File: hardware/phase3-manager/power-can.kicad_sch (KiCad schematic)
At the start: 23 parts, among them J1 BACKPLANE, Q8 2N7002, U11 TCAN1042HGV, U8 LMR36015AQRNXRQ1, U9 NCP1117-3.3

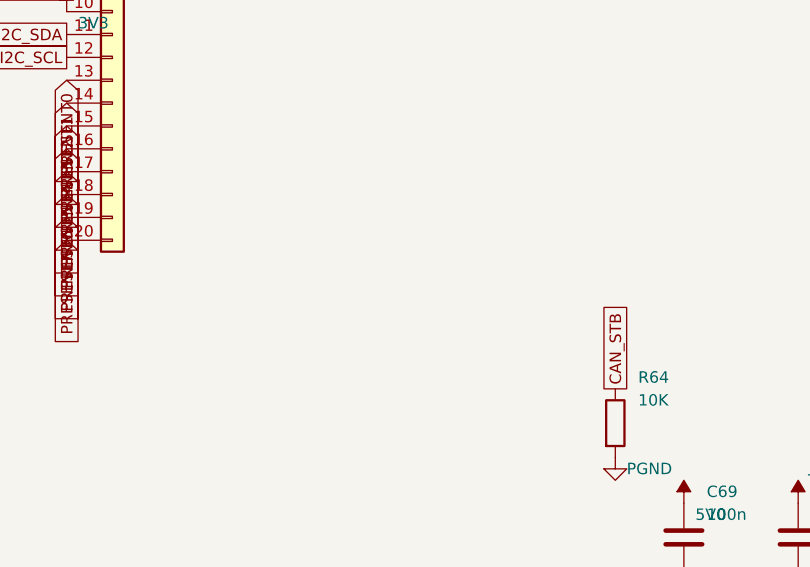
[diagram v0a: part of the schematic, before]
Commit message: Phase-3 schematic audit: real find fixed (manager I2C pull-ups), SPICE clean
The analyzer caught a genuine capture omission: docs/09 s.3 specifies 4.7K
I2C pull-ups on the manager (it owns the bus feeding TCA9535 + the
backplane INA228), but gen_manager.py never drew them - and EXPECTED_NETS,
written from the same plan, shared the blind spot. R62/R63 added, all
checkers re-verified green (80 components).

Triage of the rest:
- backplane PR-001/PU-001 "missing I2C pull-ups": by design, manager owns
  them (docs/09); U1 ALERT unused open-drain, no pull needed
- RS-001: PWR_FLAG-invisible analyzer class (accepted since Phase-1)
- SS-001/DS: MPN pass deferred to the batch BOM stage as before
ngspice: manager 16/16 pass, backplane 3/3 pass (0 warn, 0 fail, 0 skip).
Analysis manifests tracked per convention.

Co-Authored-By: Claude Fable 5 <noreply@anthropic.com>
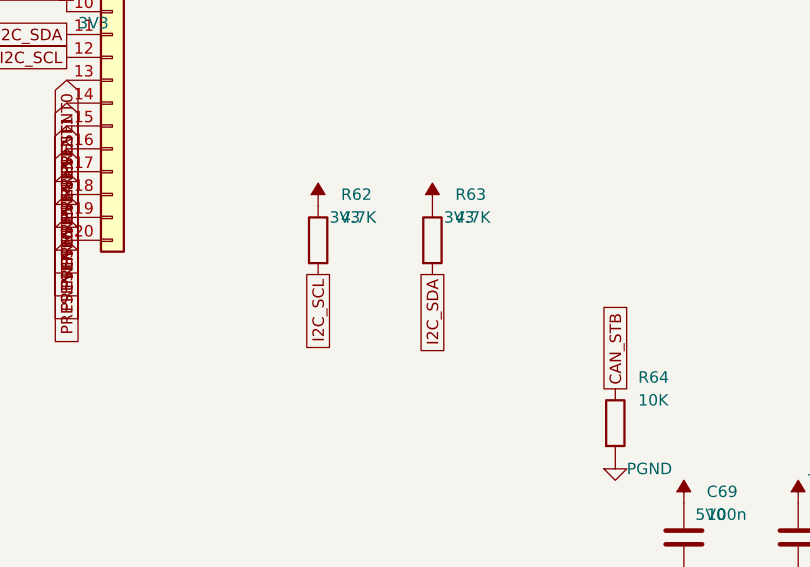
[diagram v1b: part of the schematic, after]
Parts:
- added R62, R63: 4.7K, Resistor_SMD:R_0603_1608Metric, symbol Device:R
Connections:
- net 3V3: now also R62.1, R63.1
- net I2C_SCL: now also R62.2
- net I2C_SDA: now also R63.2

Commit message: Add LCSC part numbers to all four boards' schematics and generate BOMs
common/bom.py writes hidden LCSC/MPN/Manufacturer properties into the
placed symbols (additive only, both one-line and KiCad multi-line
property styles) and emits <board>/bom/<board>-bom.csv plus a
JLCPCB-format CSV. Part table in common/lcsc_parts.py, transcribed
from SOURCING.md with explicit references per board; CHECK notes flag
footprint/variant mismatches. --check fails on stale output.

Co-Authored-By: Claude Opus 5.5 (1M context) <noreply@anthropic.com>
Claude-Session: https://claude.ai/code/session_01MKtKgebN9BpUrgqHq9t7pT
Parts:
- F1: LCSC (none) -> C3207114
- U11: LCSC (none) -> C485806; MPN (none) -> TCAN1042VDRQ1; Manufacturer (none) -> TI
- U8: LCSC (none) -> C1850345; MPN (none) -> LMR36015ARNXR; Manufacturer (none) -> TI
- U9: LCSC (none) -> C26537; MPN (none) -> NCP1117ST33T3G; Manufacturer (none) -> onsemi
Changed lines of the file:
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@@
     (property "Footprint" "Fuse:Fuse_Blade_Mini_directSolder" (at 63.5 55.88 0) (effects (font (size 1.27 1.27)) hide))
     (property "Datasheet" "~" (at 63.5 55.88 0) (effects (font (size 1.27 1.27)) hide))
+    (property "LCSC" "C3207114" (at 63.5 55.88 0) (effects (font (size 1.27 1.27)) hide))
     (pin "1")
     (pin "2")
@@
     (property "Footprint" "labbench:LMR36015_RNX_VQFN-HR-12" (at 116.84 78.74 0) (effects (font (size 1.27 1.27)) hide))
     (property "Datasheet" "~" (at 116.84 78.74 0) (effects (font (size 1.27 1.27)) hide))
+    (property "LCSC" "C1850345" (at 116.84 78.74 0) (effects (font (size 1.27 1.27)) hide))
+    (property "MPN" "LMR36015ARNXR" (at 116.84 78.74 0) (effects (font (size 1.27 1.27)) hide))
+    (property "Manufacturer" "TI" (at 116.84 78.74 0) (effects (font (size 1.27 1.27)) hide))
     (pin "1")
     (pin "10")
@@
     (property "Footprint" "Package_TO_SOT_SMD:SOT-223-3_TabPin2" (at 218.44 78.74 0) (effects (font (size 1.27 1.27)) hide))
     (property "Datasheet" "~" (at 218.44 78.74 0) (effects (font (size 1.27 1.27)) hide))
+    (property "LCSC" "C26537" (at 218.44 78.74 0) (effects (font (size 1.27 1.27)) hide))
+    (property "MPN" "NCP1117ST33T3G" (at 218.44 78.74 0) (effects (font (size 1.27 1.27)) hide))
+    (property "Manufacturer" "onsemi" (at 218.44 78.74 0) (effects (font (size 1.27 1.27)) hide))
     (pin "1")
     (pin "2")
@@
     (property "Footprint" "Package_SO:SOIC-8_3.9x4.9mm_P1.27mm" (at 116.84 152.4 0) (effects (font (size 1.27 1.27)) hide))
     (property "Datasheet" "~" (at 116.84 152.4 0) (effects (font (size 1.27 1.27)) hide))
-    (pin "1")
-    (pin "2")
+    (property "LCSC" "C485806" (at 116.84 152.4 0) (effects (font (size 1.27 1.27)) hide))
+    (property "MPN" "TCAN1042VDRQ1" (at 116.84 152.4 0) (effects (font (size 1.27 1.27)) hide))
+    (property "Manufacturer" "TI" (at 116.84 152.4 0) (effects (font (size 1.27 1.27)) hide))
+    (pin "1")
+    (pin "2")

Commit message: Fix manager ENC1, F1 and BZ1 part numbers to fit their existing lands
- ENC1: C2831776 was a 100 uF/50 V electrolytic, not an encoder. Now Alps
  EC11E18244A5 (C255515), the EC11E with push switch the footprint is for.
- F1: C3207114 was a 6.35 mm cylindrical fuse clip. The land is a
  direct-solder MINI blade, so F1 is now the 2 A fuse itself, Littelfuse
  0297002.WXNV (C151091). The Phase-1 F1 note is corrected the same way.
- BZ1: MLT-8530 is rated 2.5-4.5 V but runs from 5V0. Now YX-SMD8530P
  (C781886), rated 2-5 V, with the same vendor land and pad-1 (+) corner.

Schematic LCSC/MPN fields and BOM CSVs regenerated with common/bom.py.
No footprint or layout change.

Co-Authored-By: Claude Opus 5.5 (1M context) <noreply@anthropic.com>
Claude-Session: https://claude.ai/code/session_01Ekhw9jYnrfxihP7yvxax5H
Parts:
- F1: LCSC C3207114 -> C151091; MPN (none) -> 0297002.WXNV; Manufacturer (none) -> Littelfuse
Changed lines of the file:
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@@
     (property "Footprint" "Fuse:Fuse_Blade_Mini_directSolder" (at 63.5 55.88 0) (effects (font (size 1.27 1.27)) hide))
     (property "Datasheet" "~" (at 63.5 55.88 0) (effects (font (size 1.27 1.27)) hide))
-    (property "LCSC" "C3207114" (at 63.5 55.88 0) (effects (font (size 1.27 1.27)) hide))
+    (property "MPN" "0297002.WXNV" (at 63.5 55.88 0) (effects (font (size 1.27 1.27)) hide))
+    (property "Manufacturer" "Littelfuse" (at 63.5 55.88 0) (effects (font (size 1.27 1.27)) hide))
+    (property "LCSC" "C151091" (at 63.5 55.88 0) (effects (font (size 1.27 1.27)) hide))
     (pin "1")
     (pin "2")

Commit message: Manager L2 and backplane C2: pick stocked parts, re-route L2 as an ECO
Manager L2 (33u/1.2A aux-buck inductor) had a 1210 land, and no stocked
1210 33 uH is rated above 0.5 A. It is now the 5x5 mm cjiang
FNR5040S330MT (C167973: Isat 1.30 A min, Irms 1.20 A min, 0.244 ohm)
on KiCad's L_Changjiang_FNR5040S land.

Board ECO, no full re-route:
- L2 moves to (18.8, 48.4) so its courtyard clears C54, F1 and C50/C51;
  C54/C55 turn 180 so their 5V0 pads line up with L2's 5V0 pad (one
  straight 0.8 mm run) and their PGND pads are tied and dropped to the
  plane west of C55.
- SW_AUX and the 5V0 head are redrawn locked, matching route_critical.py;
  PRESENT1/4-7 are re-routed round the bigger part by finish_routes.py.
- gen_board.py PLACEMENT and route_critical.py ROUTES carry the same
  change, so a full rebuild reproduces it.
- DRC: 0 unconnected, 0 errors, 4 warnings (was 5). Fab zip, BOM, CPL
  regenerated.

Backplane C2 (470u/50V on CP_Elec_16x17.5): Nichicon UCX1H471MNS1MS
(C462700, 16x16.5, 70 mOhm), which fits the existing land; Panasonic
EEEFK1H471AM (C178551) is the fallback. No board change.

Co-Authored-By: Claude Opus 5.5 (1M context) <noreply@anthropic.com>
Claude-Session: https://claude.ai/code/session_016Wr11AqV5ZRbpysgP42oHy
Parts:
- L2: footprint Inductor_SMD:L_1210_3225Metric -> Inductor_SMD:L_Changjiang_FNR5040S; LCSC (none) -> C167973; MPN (none) -> FNR5040S330MT; Manufacturer (none) -> cjiang (Changjiang Microelectronics)
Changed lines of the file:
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@@
     (property "Reference" "L2" (at 153.67 87.63 0) (effects (font (size 1.27 1.27))))
     (property "Value" "33u/1.2A" (at 153.67 95.25 0) (effects (font (size 1.27 1.27))))
-    (property "Footprint" "Inductor_SMD:L_1210_3225Metric" (at 153.67 91.44 0) (effects (font (size 1.27 1.27)) hide))
+    (property "Footprint" "Inductor_SMD:L_Changjiang_FNR5040S" (at 153.67 91.44 0) (effects (font (size 1.27 1.27)) hide))
     (property "Datasheet" "~" (at 153.67 91.44 0) (effects (font (size 1.27 1.27)) hide))
+    (property "LCSC" "C167973" (at 153.67 91.44 0) (effects (font (size 1.27 1.27)) hide))
+    (property "MPN" "FNR5040S330MT" (at 153.67 91.44 0) (effects (font (size 1.27 1.27)) hide))
+    (property "Manufacturer" "cjiang (Changjiang Microelectronics)" (at 153.67 91.44 0) (effects (font (size 1.27 1.27)) hide))
     (pin "1")
     (pin "2")
